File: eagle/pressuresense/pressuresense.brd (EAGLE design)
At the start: 25.4 x 25.4 mm, 7 parts

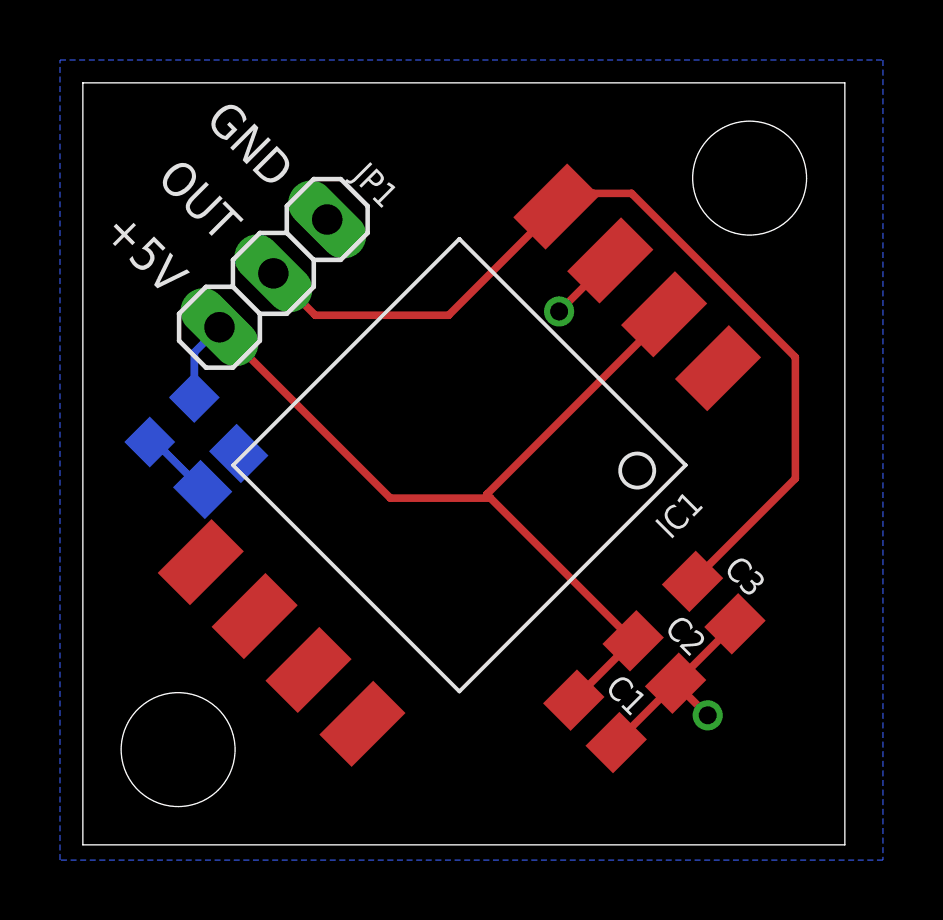
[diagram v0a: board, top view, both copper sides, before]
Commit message: Finalized pressure sensor board. Sent rev 6.10.14 for production.
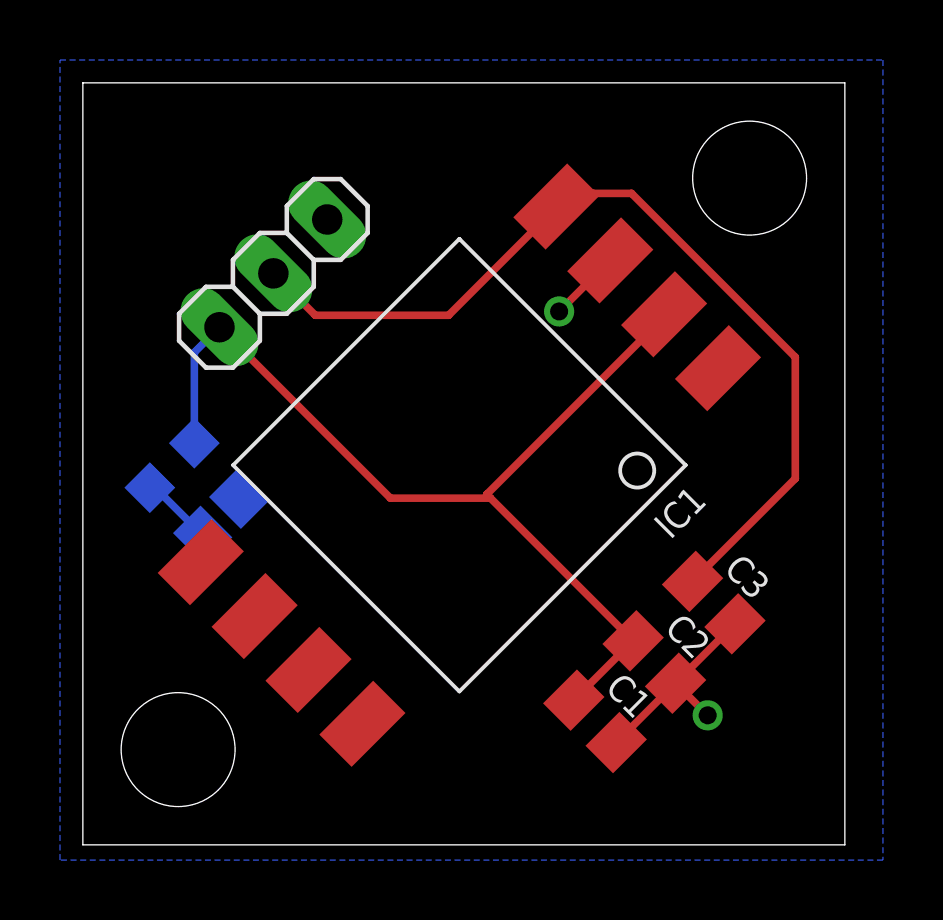
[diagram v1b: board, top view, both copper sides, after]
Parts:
- moved LED1 1.52 mm to (2.97, 12.6)
- moved R1 1.52 mm to (4.59, 10.9)
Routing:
- net VCC: track 32.2 -> 33.8 mm
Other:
- board text added: "AUVUA"
- board text added: "R1"
- board text added: "pressure sensor"
- board text added: "rev 6.10.14"
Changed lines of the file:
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@@
 <?xml version="1.0" encoding="utf-8"?>
 <!DOCTYPE eagle SYSTEM "eagle.dtd">
-<eagle version="6.4">
+<eagle version="6.5.0">
 <drawing>
 <settings>
@@
 <layer number="20" name="Dimension" color="15" fill="1" visible="yes" active="yes"/>
 <layer number="21" name="tPlace" color="7" fill="1" visible="yes" active="yes"/>
-<layer number="22" name="bPlace" color="7" fill="1" visible="no" active="yes"/>
+<layer number="22" name="bPlace" color="7" fill="1" visible="yes" active="yes"/>
 <layer number="23" name="tOrigins" color="15" fill="1" visible="yes" active="yes"/>
 <layer number="24" name="bOrigins" color="15" fill="1" visible="yes" active="yes"/>
@@
 <hole x="3.175" y="3.175" drill="3.7973"/>
 <hole x="22.225" y="22.225" drill="3.7973"/>
-<text x="6.731" y="22.225" size="1.143" layer="21" rot="R135" align="center-left">GND</text>
-<text x="4.953" y="20.447" size="1.143" layer="21" rot="R135" align="center-left">OUT</text>
-<text x="3.175" y="18.669" size="1.143" layer="21" rot="R135" align="center-left">+5V</text>
+<text x="14.986" y="22.352" size="1.143" layer="22" ratio="10" rot="MR45" align="center-left">GND</text>
+<text x="14.097" y="21.463" size="1.143" layer="22" ratio="10" rot="MR45" align="center-left">OUT</text>
+<text x="13.208" y="20.574" size="1.143" layer="22" ratio="10" rot="MR45" align="center-left">+5V</text>
+<text x="4.826" y="9.271" size="0.889" layer="22" ratio="10" rot="MR135">R1</text>
+<text x="24.257" y="4.953" size="1.524" layer="22" ratio="10" rot="MR0">AUVUA</text>
+<text x="24.257" y="2.667" size="1.27" layer="22" ratio="10" rot="MR0">pressure sensor</text>
+<text x="24.257" y="0.762" size="1.27" layer="22" ratio="10" rot="MR0">rev 6.10.14</text>
 </plain>
 <attributes>
@@
 <elements>
 <element name="IC1" library="custom" package="MPXA4250AC6U" value="" x="12.551209375" y="12.65641875" smashed="yes" rot="R45">
-<attribute name="NAME" x="19.581978125" y="10.14723125" size="0.8128" layer="21" rot="R45"/>
+<attribute name="NAME" x="19.581978125" y="10.14723125" size="0.889" layer="21" ratio="10" rot="R45"/>
 </element>
 <element name="JP1" library="pinhead" package="1X03" value="" x="6.35" y="19.05" smashed="yes" rot="R45">
-<attribute name="NAME" x="10.598803125" y="21.7398875" size="0.8128" layer="25" ratio="10" rot="R135"/>
 <attribute name="VALUE" x="5.900984375" y="14.11085625" size="1.27" layer="27" rot="R45"/>
 </element>
 <element name="C1" library="resistor" package="C0805K" value="1uF" x="17.070603125" y="4.11660625" smashed="yes" rot="R315">
-<attribute name="NAME" x="17.3632125" y="5.18843125" size="0.8128" layer="25" rot="R315"/>
+<attribute name="NAME" x="17.3632125" y="5.18843125" size="0.889" layer="25" ratio="10" rot="R315"/>
 <attribute name="VALUE" x="15.019990625" y="3.480209375" size="1.016" layer="27" rot="R315"/>
 </element>
 <element name="C2" library="resistor" package="C0805K" value="0.01uF" x="19.05" y="6.096" smashed="yes" rot="R315">
-<attribute name="NAME" x="19.342609375" y="7.167825" size="0.8128" layer="25" rot="R315"/>
+<attribute name="NAME" x="19.342609375" y="7.167825" size="0.889" layer="25" ratio="10" rot="R315"/>
 <attribute name="VALUE" x="16.9993875" y="5.459603125" size="1.016" layer="27" rot="R315"/>
 </element>
 <element name="C3" library="resistor" package="C0805K" value="470pF" x="21.02939375" y="8.075396875" smashed="yes" rot="R315">
-<attribute name="NAME" x="21.322003125" y="9.147221875" size="0.8128" layer="25" rot="R315"/>
+<attribute name="NAME" x="21.322003125" y="9.147221875" size="0.889" layer="25" ratio="10" rot="R315"/>
 <attribute name="VALUE" x="18.97878125" y="7.439" size="1.016" layer="27" rot="R315"/>
 </element>
-<element name="R1" library="resistor" package="R0805" value="220" x="4.593790625" y="12.446" smashed="yes" rot="MR315">
-<attribute name="NAME" x="4.2871875" y="13.449234375" size="0.8128" layer="26" rot="MR315"/>
-<attribute name="VALUE" x="6.749053125" y="11.36836875" size="1.27" layer="28" rot="MR315"/>
-</element>
-<element name="LED1" library="led" package="CHIP-LED0805" value="" x="2.97360625" y="14.171396875" smashed="yes" rot="MR225">
-<attribute name="VALUE" x="5.667684375" y="13.27336875" size="1.27" layer="28" rot="MR315"/>
-</element>
+<element name="R1" library="resistor" package="R0805" value="220" x="4.593790625" y="10.922" rot="MR315"/>
+<element name="LED1" library="led" package="CHIP-LED0805" value="" x="2.97360625" y="12.647396875" rot="MR225"/>
 </elements>
 <signals>
@@
 <wire x1="18.342890625" y1="6.80310625" x2="16.36349375" y2="4.8237125" width="0.254" layer="1"/>
 <wire x1="19.376203125" y1="17.598203125" x2="19.376203125" y2="17.685359375" width="0.254" layer="1"/>
-<wire x1="3.71606875" y1="14.91385625" x2="3.71606875" y2="16.41606875" width="0.254" layer="16"/>
+<wire x1="3.71606875" y1="13.38985625" x2="3.71606875" y2="16.41606875" width="0.254" layer="16"/>
 <wire x1="3.71606875" y1="16.41606875" x2="4.553946875" y2="17.253946875" width="0.254" layer="16"/>
 <wire x1="18.342890625" y1="6.80310625" x2="13.588996875" y2="11.557" width="0.254" layer="1"/>
@@
 <contactref element="C3" pad="2"/>
 <contactref element="R1" pad="1"/>
-<polygon width="0.4064" layer="16">
+<polygon width="0.254" layer="16">
 <vertex x="-0.762" y="26.162"/>
 <vertex x="26.67" y="26.162"/>
@@
 <contactref element="LED1" pad="C"/>
 <contactref element="R1" pad="2"/>
-<wire x1="2.231146875" y1="13.428934375" x2="2.408771875" y2="13.428934375" width="0.254" layer="16"/>
-<wire x1="2.408771875" y1="13.428934375" x2="3.99275" y2="11.84495625" width="0.254" layer="16"/>
+<wire x1="2.231146875" y1="11.904934375" x2="2.408771875" y2="11.904934375" width="0.254" layer="16"/>
+<wire x1="2.408771875" y1="11.904934375" x2="3.99275" y2="10.32095625" width="0.254" layer="16"/>
 </signal>
 </signals>
